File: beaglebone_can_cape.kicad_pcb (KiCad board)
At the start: 2 copper layers, 86.4 x 54.6 mm, 30 parts, among them J1 Conn_01x02_Pin, J2 Conn_01x02_Pin, J3 DTM15-12PA, J4 Conn_02x02_Top_Bottom, J5 Battery Harness, P8 BeagleBone_Black_Header, P9 BeagleBone_Black_Header, U1 TCAN332, U2 TCAN332, U3 LMR51430

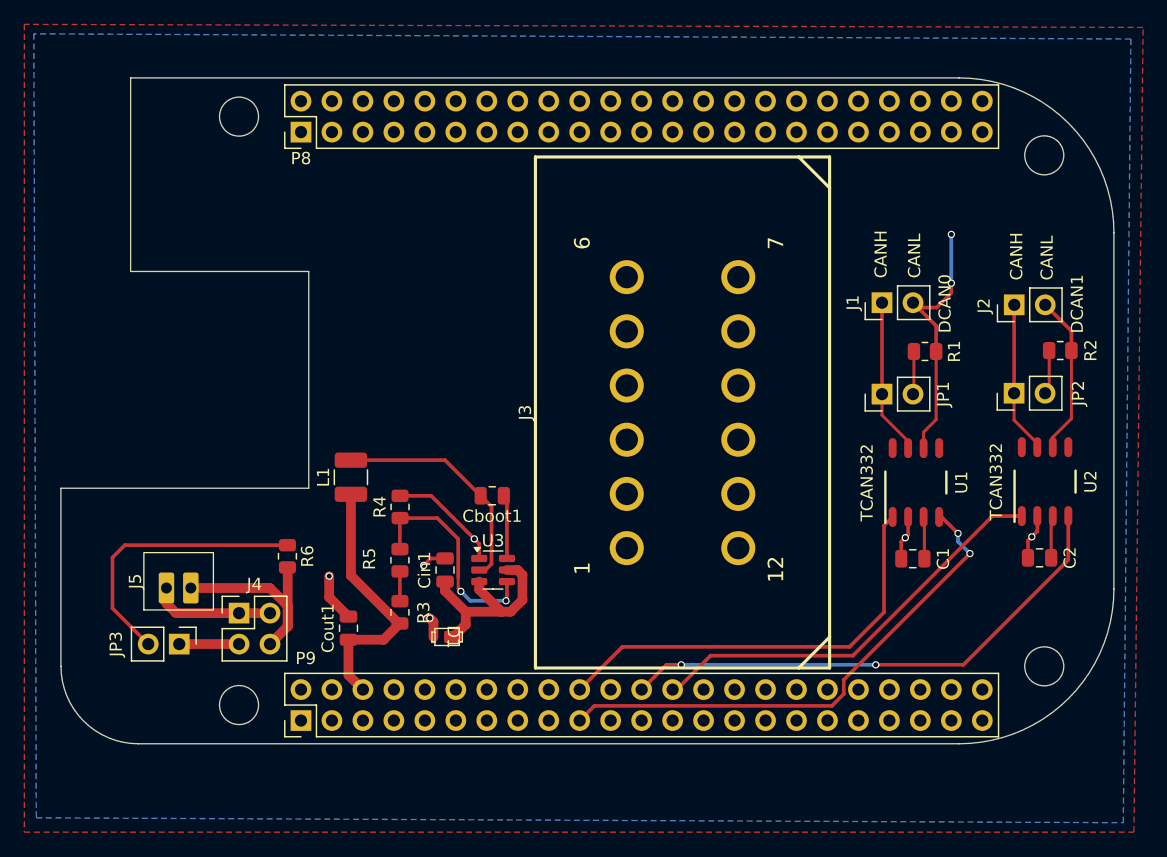
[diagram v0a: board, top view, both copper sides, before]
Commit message: Implementing Deutsch + wiring
* Got rid of more errors and corrected more footprints. Going smoothly.
* Researched the TVS diode. cool stuff!
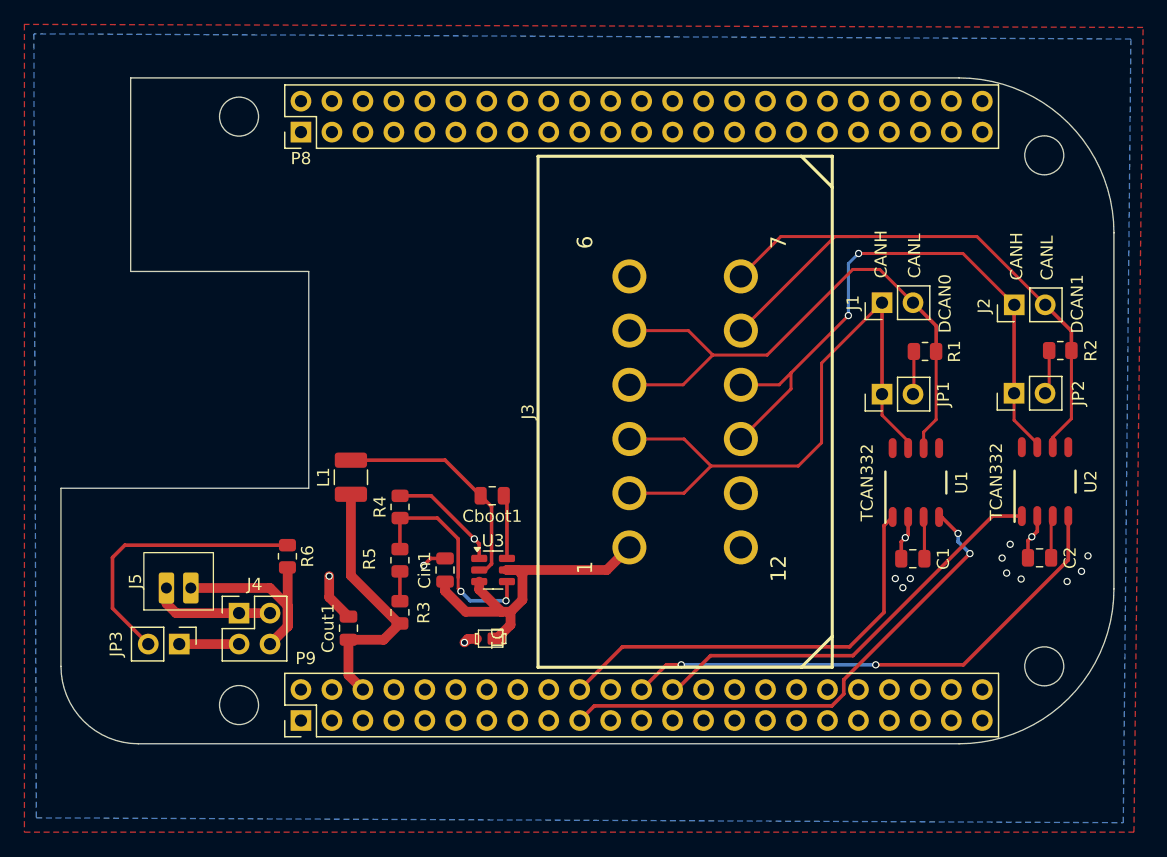
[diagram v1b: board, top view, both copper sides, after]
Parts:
- moved D1 3.57 mm to (135.2, 91.4)
- moved J3 0.22 mm to (151.2, 72.8)
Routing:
- net CAN LOW 1: track 13.2 -> 54.7 mm
- net CAN HIGH 0: track 12.8 -> 51.4 mm
- net CAN HIGH 1: track 12.5 -> 50.7 mm, vias 0 -> 2
- net CAN LOW 0: track 21.7 -> 49.7 mm, vias 2 -> 0
- net +24V: track 17.4 -> 28.4 mm
- net GND: track 24.4 -> 23.8 mm, vias 6 -> 16

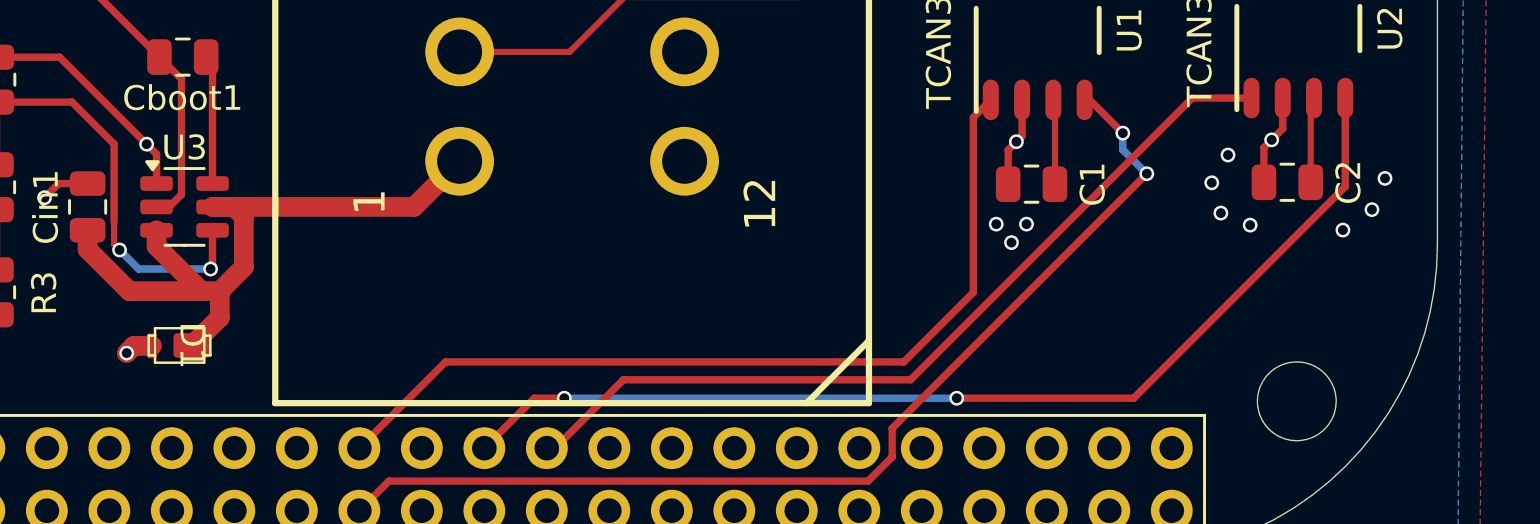
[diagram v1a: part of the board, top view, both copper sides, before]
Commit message: PCB updates
Wiring and moving TVS and Deutsch
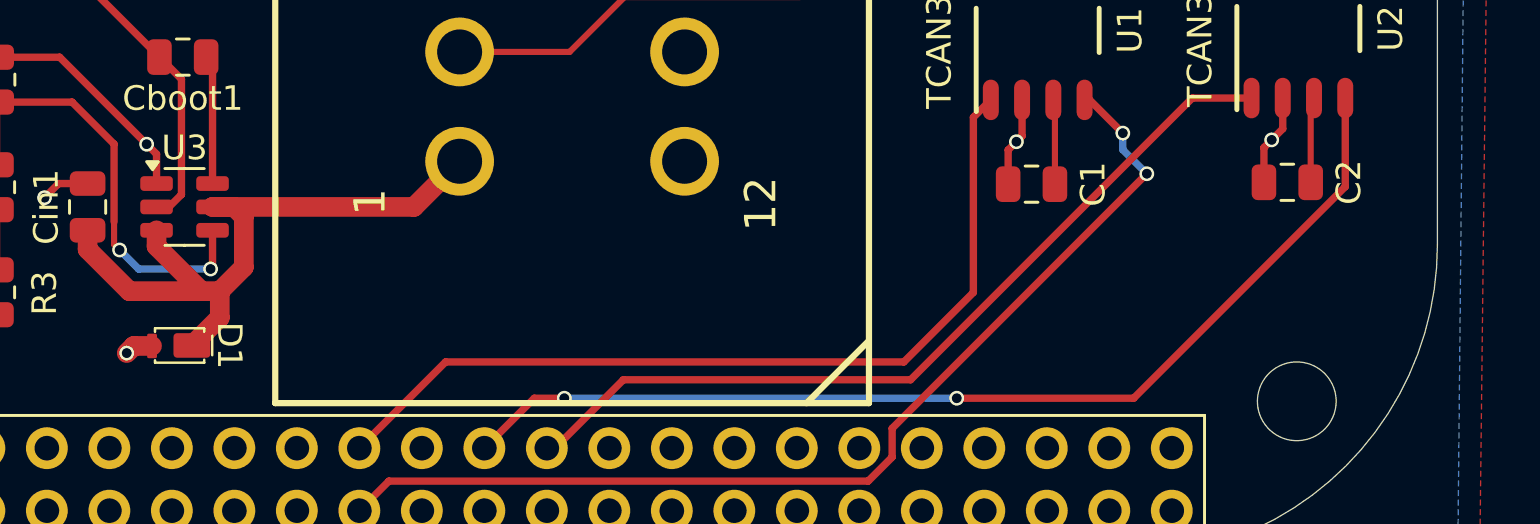
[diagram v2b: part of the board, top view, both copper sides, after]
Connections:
- P9 pad 3: +3V3 -> +3.3V
- P9 pad 4: +3V3 -> +3.3V
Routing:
- net GND: vias 16 -> 6

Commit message: pushing pwr_flag and ERC changes
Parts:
- moved U3 1.12 mm to (135.1, 84.7), turned to -90 degrees
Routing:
- net +24V: track 28.4 -> 36.8 mm, vias 0 -> 2
- net Net-(U3-FB): track 18.1 -> 11.3 mm, vias 2 -> 0
- net GND: track 23.8 -> 19.0 mm, vias 6 -> 7
- net Net-(U3-SW): track 19.0 -> 16.0 mm
- net Net-(U3-CB): track 5.25 -> 7.52 mm

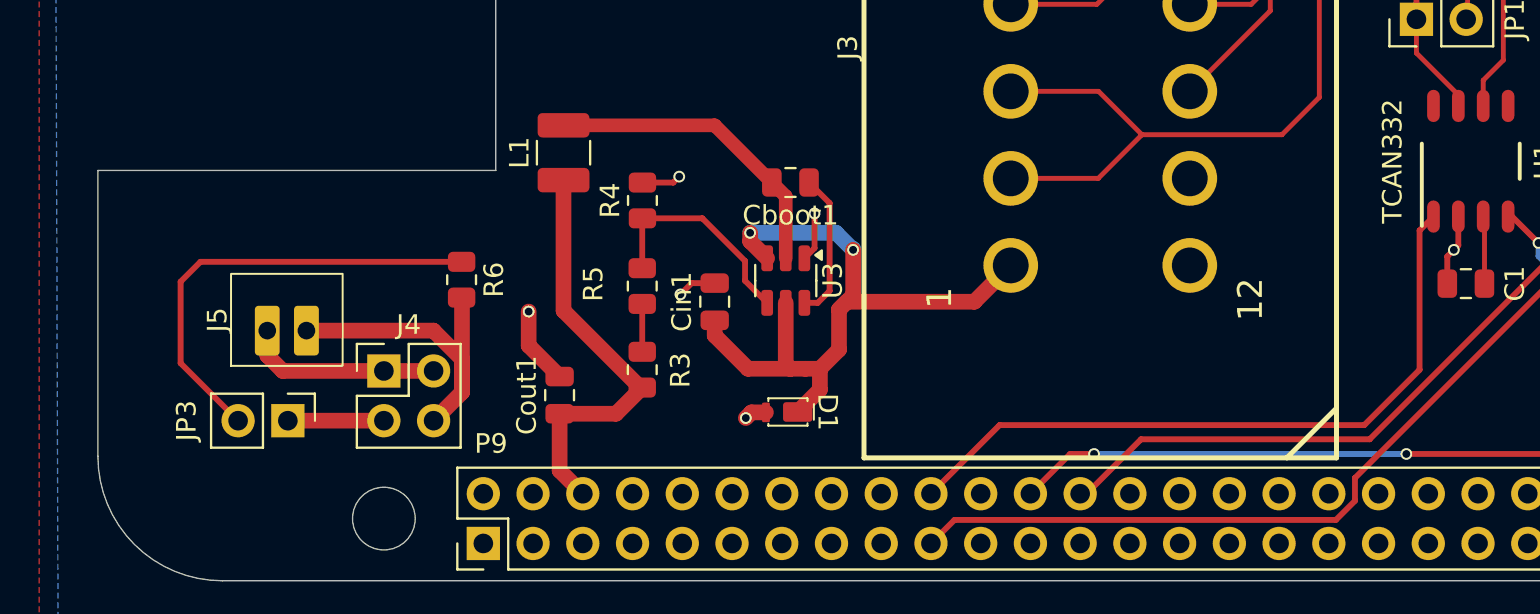
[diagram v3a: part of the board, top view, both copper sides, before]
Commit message: Before-Meeting final PCB and Schematic changes
* Redid the battery circuit to be... yk... correct because I wired it wrong the first time lols
* I changed the width of all high voltage & current lines to 0.8mm, really no big change there, nothing had to be moved
* Looked in depth at anything missing, I think we're just about good to go
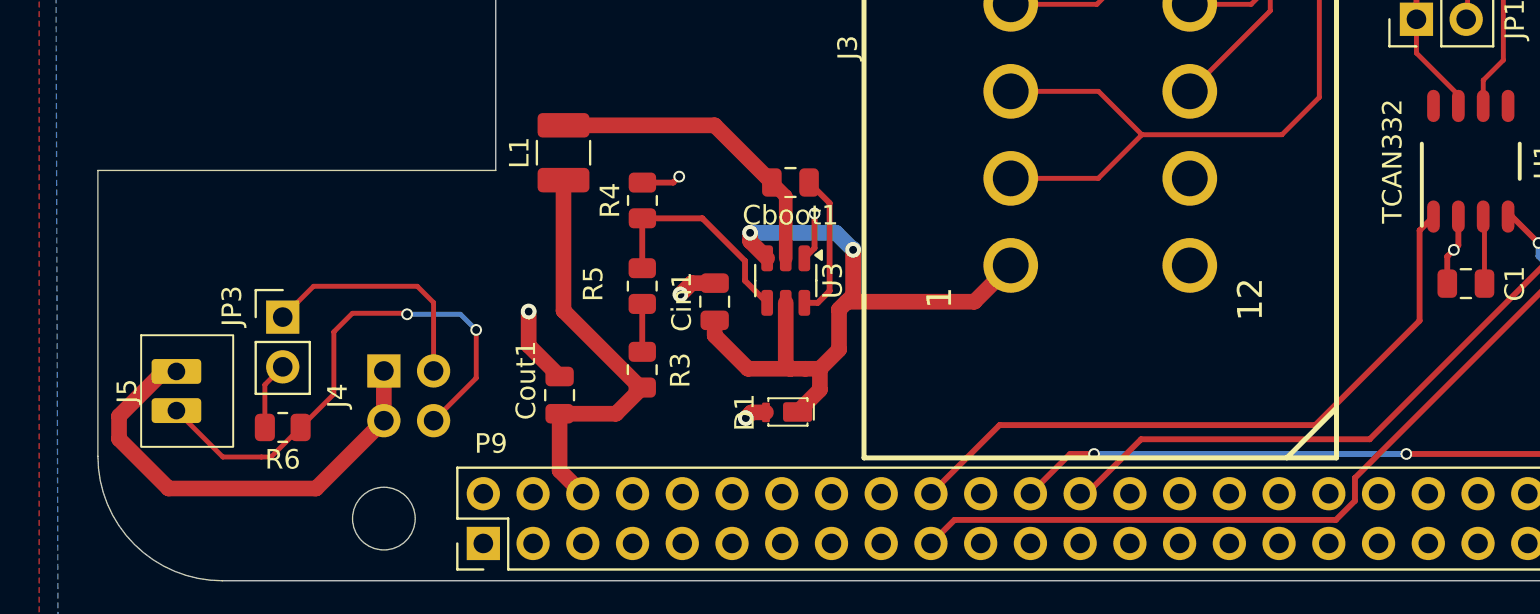
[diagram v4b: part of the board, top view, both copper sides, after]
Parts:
- J4: moved to B.Cu
- moved R6 11.8 mm to (109.4, 92.2), turned to 0 degrees
- moved J5 6.25 mm to (104.6, 90.3), turned to 0 degrees
- moved JP3 5.30 mm to (109.4, 86.5), turned to 0 degrees
- turned J4 to -90 degrees
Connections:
- P8 pad 1: GNDD -> GND
- P8 pad 2: GNDD -> GND
- P9 pad 1: GNDD -> GND
- P9 pad 2: GNDD -> GND
- P9 pad 43: GNDD -> GND
- P9 pad 44: GNDD -> GND
- P9 pad 45: GNDD -> GND
- P9 pad 46: GNDD -> GND
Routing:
- net Net-(JP3-B): track 23.1 -> 3.47 mm
- net Net-(J4-Pin_1): track 10.1 -> 23.6 mm
- net Net-(J4-Pin_4): track 17.1 -> 27.1 mm, vias 0 -> 2
- net Net-(J4-Pin_3): track 4.91 -> 12.2 mm
- net /I2C2.SDA: track 36.2 -> 34.7 mm

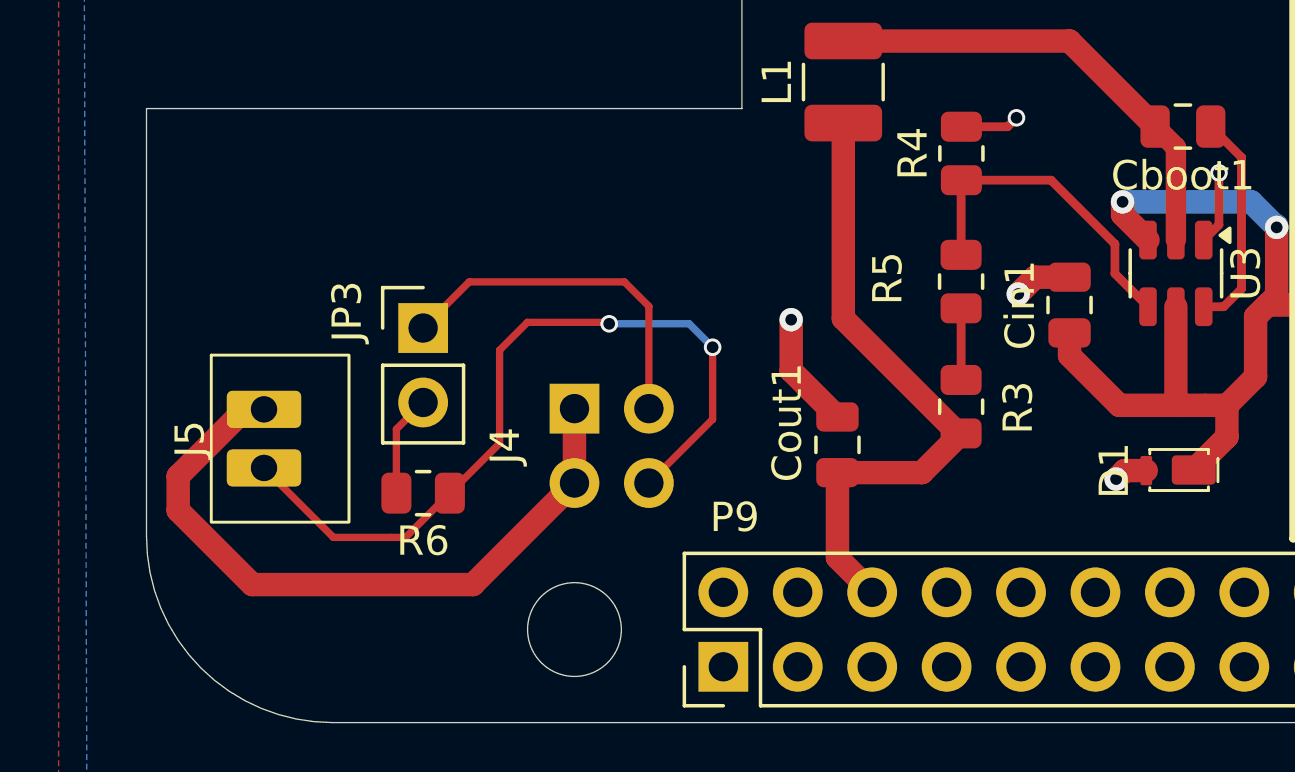
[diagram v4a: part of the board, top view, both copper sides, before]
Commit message: Joey request LED + battery harness things
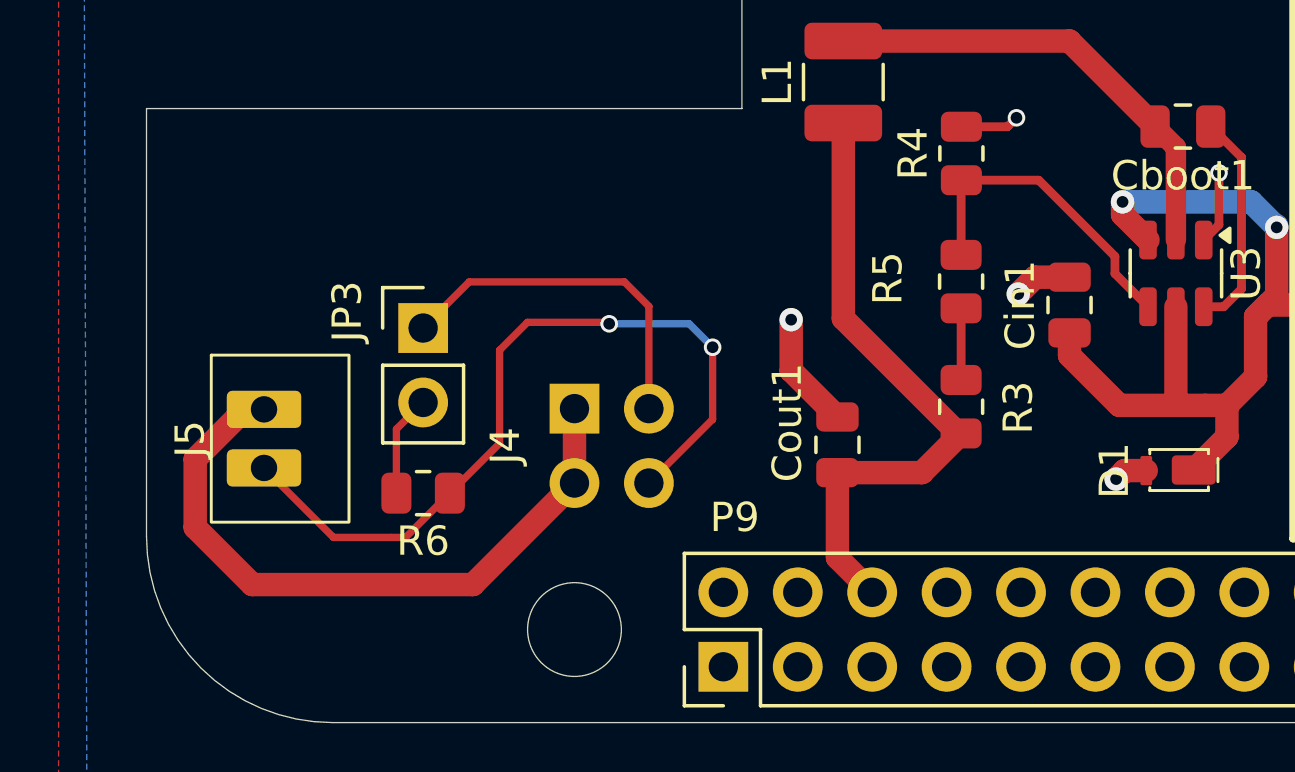
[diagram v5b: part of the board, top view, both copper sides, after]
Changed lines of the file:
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@@
+	)
+	(segment
+		(start 178.17 73.46)
+		(end 178.17 71.25)
+		(width 0.25)
+		(layer "F.Cu")
+		(net 7)
+	)
+	(segment
+		(start 178.17 64.015)
+		(end 178.185 64)
+		(width 0.3)
+		(layer "F.Cu")
+		(net 7)
+	)
+	(segment
+		(start 173.975 59.79)
+		(end 178.185 64)
+		(width 0.25)
+		(layer "F.Cu")
+		(net 7)
+	)
+	(segment
+		(start 159.875 69.585)
+		(end 164.42 65.04)
+		(width 0.25)
+		(layer "F.Cu")
+		(net 7)
+	)
+	(segment
+		(start 178.17 71.25)
+		(end 178.17 64.015)
+		(width 0.3)
+		(layer "F.Cu")
+		(net 7)
+	)
+	(segment
+		(start 159.875 70.894)
+		(end 159.875 69.585)
+		(width 0.25)
+		(layer "F.Cu")
+		(net 7)
+	)
+	(segment
+		(start 180.075 75.365)
+		(end 178.17 73.46)
+		(width 0.25)
+		(layer "F.Cu")
+		(net 7)
 	)
 	(segment
 		(start 155.764 75.005)
 		(end 159.875 70.894)
-		(width 0.25)
-		(layer "F.Cu")
-		(net 7)
-	)
-	(segment
-		(start 178.17 73.46)
-		(end 178.17 71.25)
-		(width 0.25)
-		(layer "F.Cu")
-		(net 7)
-	)
-	(segment
-		(start 178.17 64.015)
-		(end 178.185 64)
-		(width 0.3)
-		(layer "F.Cu")
-		(net 7)
-	)
-	(segment
-		(start 173.975 59.79)
-		(end 178.185 64)
-		(width 0.25)
-		(layer "F.Cu")
-		(net 7)
-	)
-	(segment
-		(start 159.875 70.894)
-		(end 159.875 69.585)
-		(width 0.25)
-		(layer "F.Cu")
-		(net 7)
-	)
-	(segment
-		(start 159.875 69.585)
-		(end 164.42 65.04)
-		(width 0.25)
-		(layer "F.Cu")
-		(net 7)
-	)
-	(segment
-		(start 178.17 71.25)
-		(end 178.17 64.015)
-		(width 0.3)
-		(layer "F.Cu")
-		(net 7)
-	)
-	(segment
-		(start 180.075 75.365)
-		(end 178.17 73.46)
 		(width 0.25)
 		(layer "F.Cu")
@@
 	)
 	(segment
-		(start 133.05 83.67)
-		(end 133.05 84.6775)
-		(width 0.3)
-		(layer "F.Cu")
-		(net 16)
-	)
-	(segment
 		(start 133.05 84.6775)
 		(end 134.18 85.8075)
@@
 	)
 	(segment
-		(start 130.87 81.49)
-		(end 133.05 83.67)
+		(start 130.45 81.49)
+		(end 133.05 84.09)
+		(width 0.3)
+		(layer "F.Cu")
+		(net 16)
+	)
+	(segment
+		(start 127.81 81.49)
+		(end 130.45 81.49)
+		(width 0.3)
+		(layer "F.Cu")
+		(net 16)
+	)
+	(segment
+		(start 133.05 84.09)
+		(end 133.05 84.6775)
 		(width 0.3)
 		(layer "F.Cu")
@@
 	)
 	(segment
-		(start 127.81 81.49)
-		(end 130.87 81.49)
-		(width 0.3)
-		(layer "F.Cu")
-		(net 16)
-	)
-	(segment
 		(start 127.8 81.5)
 		(end 127.81 81.49)
@@
 	)
 	(segment
+		(start 114.605 91.825)
+		(end 111.14 95.29)
+		(width 0.8)
+		(layer "F.Cu")
+		(net 22)
+	)
+	(segment
+		(start 101.66 91.01137)
+		(end 103.36137 89.31)
+		(width 0.8)
+		(layer "F.Cu")
+		(net 22)
+	)
+	(segment
+		(start 103.36137 89.31)
+		(end 104.01 89.31)
+		(width 0.8)
+		(layer "F.Cu")
+		(net 22)
+	)
+	(segment
+		(start 101.66 93.34)
+		(end 101.66 91.01137)
+		(width 0.8)
+		(layer "F.Cu")
+		(net 22)
+	)
+	(segment
+		(start 114.605 89.285)
+		(end 114.605 91.825)
+		(width 0.8)
+		(layer "F.Cu")
+		(net 22)
+	)
+	(segment
 		(start 111.14 95.29)
 		(end 103.61 95.29)
@@
 	)
 	(segment
-		(start 114.605 91.825)
-		(end 111.14 95.29)
-		(width 0.8)
-		(layer "F.Cu")
-		(net 22)
-	)
-	(segment
-		(start 101.08 91.59137)
-		(end 103.36137 89.31)
-		(width 0.8)
-		(layer "F.Cu")
-		(net 22)
-	)
-	(segment
-		(start 103.36137 89.31)
-		(end 104.01 89.31)
-		(width 0.8)
-		(layer "F.Cu")
-		(net 22)
-	)
-	(segment
 		(start 103.61 95.29)
-		(end 101.08 92.76)
-		(width 0.8)
-		(layer "F.Cu")
-		(net 22)
-	)
-	(segment
-		(start 101.08 92.76)
-		(end 101.08 91.59137)
-		(width 0.8)
-		(layer "F.Cu")
-		(net 22)
-	)
-	(segment
-		(start 114.605 89.285)
-		(end 114.605 91.825)
-		(width 0.8)
-		(layer "F.Cu")
+		(end 101.66 93.34)
+		(width 0.8)
+		(layer "F.Cu")

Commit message: pushing changes
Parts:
- added D2: CAN0LED, LED_SMD:LED_0805_2012Metric, F.Cu at (169.2, 55.5)
- added D3: CAN1LED, LED_SMD:LED_0805_2012Metric, F.Cu at (183.3, 89.3)
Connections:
- J4 pad 4: Net-(J4-Pin_4) -> GND
- J5 pad 2: Net-(J4-Pin_4) -> GND
- P9 pad 21: unconnected-(P9-Pin_21-Pad21) -> /GPIO3
- P9 pad 22: unconnected-(P9-Pin_22-Pad22) -> /GPIO2
- R6 pad 2: Net-(J4-Pin_4) -> GND
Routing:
- net /GPIO2: track 0.00 -> 59.7 mm, vias 0 -> 1
- net /GPIO3: track 0.00 -> 44.7 mm, vias 0 -> 1
- net Net-(J4-Pin_4): track 27.1 -> 0.00 mm, vias 2 -> 0
- net GND: track 19.0 -> 23.3 mm, vias 7 -> 10
